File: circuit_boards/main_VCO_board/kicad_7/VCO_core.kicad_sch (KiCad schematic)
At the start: 46 parts, among them Q201 MMBT3904, SW2 SR1712F-0204, U1004 LM4040C-2.5, U6 SSI2130, U7 TL072

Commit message: Progress on circuit boards
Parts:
- R1001: value ? -> 1k
- R214: value ? -> 39k
- R215: value ? -> 47k
- R216, R217: value ? -> 2M2
- RV201: value ? -> 5k
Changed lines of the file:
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@@
   (title_block
     (title "MICRO-OX Main VCO board")
-    (date "2023-03-27")
+    (date "2023-04-12")
     (rev "0")
     (comment 2 "creativecommons.org/licenses/by/4.0")
@@
   )
   (text_box "Sync \"kick start\" circuit to ensure that the VCO starts up.\n\nSee Sound Semiconductor AB503 application brief."
-    (at 15.24 25.4 0) (size 29.21 21.59)
+    (at 15.24 25.4 0) (size 29.21 26.67)
     (stroke (width 0) (type default))
     (fill (type none))
@@
   (symbol (lib_id "Device:R") (at 86.36 173.99 270) (unit 1)
     (in_bom yes) (on_board yes) (dnp no) (fields_autoplaced)
-    (property "Reference" "R216" (at 86.36 167.64 90)
-      (effects (font (size 1.27 1.27)))
-    )
-    (property "Value" "?" (at 86.36 170.18 90)
+    (property "Reference" "R216" (at 86.36 168.91 90)
+      (effects (font (size 1.27 1.27)))
+    )
+    (property "Value" "2M2" (at 86.36 171.45 90)
       (effects (font (size 1.27 1.27)))
     )
@@
   (symbol (lib_id "Device:R_Potentiometer_Trim") (at 69.85 161.29 270) (unit 1)
     (in_bom yes) (on_board yes) (dnp no) (fields_autoplaced)
-    (property "Reference" "RV201" (at 69.85 154.94 90)
-      (effects (font (size 1.27 1.27)))
-    )
-    (property "Value" "?" (at 69.85 157.48 90)
+    (property "Reference" "RV201" (at 69.85 156.21 90)
+      (effects (font (size 1.27 1.27)))
+    )
+    (property "Value" "5k" (at 69.85 158.75 90)
       (effects (font (size 1.27 1.27)))
     )
@@
   (symbol (lib_id "Device:R") (at 86.36 147.32 270) (unit 1)
     (in_bom yes) (on_board yes) (dnp no) (fields_autoplaced)
-    (property "Reference" "R214" (at 86.36 140.97 90)
-      (effects (font (size 1.27 1.27)))
-    )
-    (property "Value" "?" (at 86.36 143.51 90)
+    (property "Reference" "R214" (at 86.36 142.24 90)
+      (effects (font (size 1.27 1.27)))
+    )
+    (property "Value" "39k" (at 86.36 144.78 90)
       (effects (font (size 1.27 1.27)))
     )
@@
   (symbol (lib_id "Device:R") (at 86.36 161.29 270) (unit 1)
     (in_bom yes) (on_board yes) (dnp no) (fields_autoplaced)
-    (property "Reference" "R215" (at 86.36 154.94 90)
-      (effects (font (size 1.27 1.27)))
-    )
-    (property "Value" "?" (at 86.36 157.48 90)
+    (property "Reference" "R215" (at 86.36 156.21 90)
+      (effects (font (size 1.27 1.27)))
+    )
+    (property "Value" "47k" (at 86.36 158.75 90)
       (effects (font (size 1.27 1.27)))
     )
@@
   (symbol (lib_id "Device:R") (at 86.36 185.42 270) (unit 1)
     (in_bom yes) (on_board yes) (dnp no) (fields_autoplaced)
-    (property "Reference" "R217" (at 86.36 179.07 90)
-      (effects (font (size 1.27 1.27)))
-    )
-    (property "Value" "?" (at 86.36 181.61 90)
+    (property "Reference" "R217" (at 86.36 180.34 90)
+      (effects (font (size 1.27 1.27)))
+    )
+    (property "Value" "2M2" (at 86.36 182.88 90)
       (effects (font (size 1.27 1.27)))
     )
@@
   (symbol (lib_id "Device:R") (at 128.27 163.83 0) (unit 1)
     (in_bom yes) (on_board yes) (dnp no) (fields_autoplaced)
-    (property "Reference" "R1001" (at 130.81 162.56 0)
-      (effects (font (size 1.27 1.27)) (justify left))
-    )
-    (property "Value" "?" (at 130.81 165.1 0)
-      (effects (font (size 1.27 1.27)) (justify left))
-    )
+    (property "Reference" "R1001" (at 130.81 163.195 0)
+      (effects (font (size 1.27 1.27)) (justify left))
+    )
+    (property "Value" "1k" (at 130.81 165.735 0)
+      (effects (font (size 1.27 1.27)) (justify left))
+    )

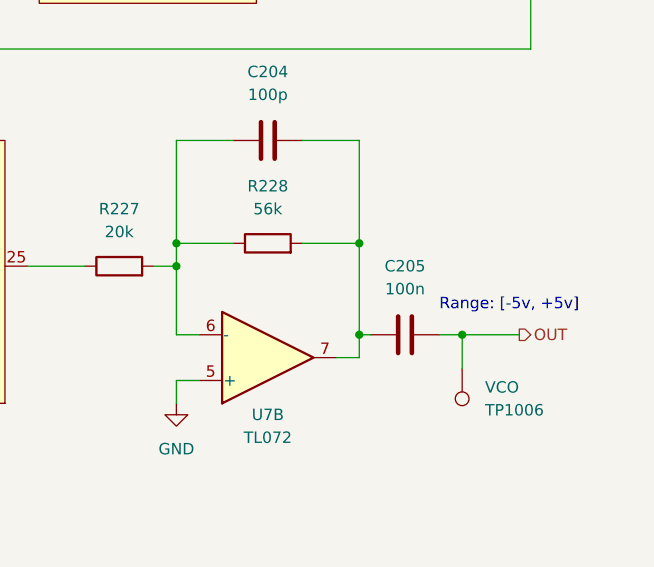
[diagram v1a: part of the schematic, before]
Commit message: Update PCBs, tweak vals, add VCF CV from DAC
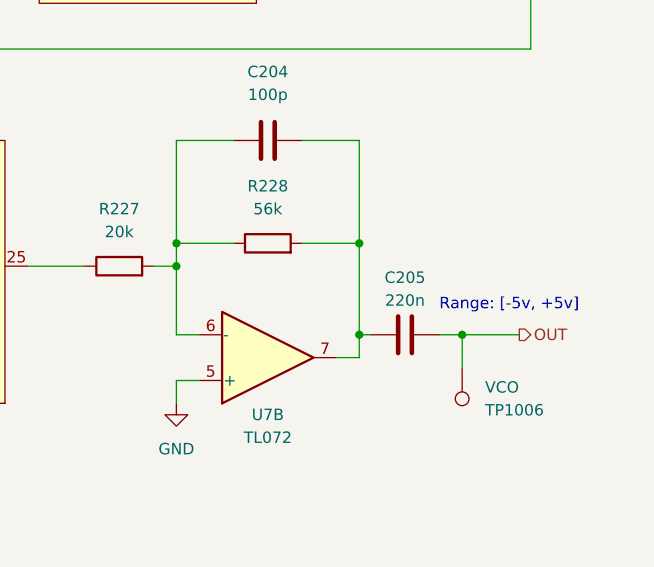
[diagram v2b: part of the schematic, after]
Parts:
- C205: value 100n -> 220n
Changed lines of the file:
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@@
   (symbol (lib_id "Device:C") (at 262.89 146.05 90) (unit 1)
     (in_bom yes) (on_board yes) (dnp no) (fields_autoplaced)
-    (property "Reference" "C205" (at 262.89 138.43 90)
+    (property "Reference" "C205" (at 262.89 139.7 90)
       (effects (font (size 1.27 1.27)))
     )
-    (property "Value" "100n" (at 262.89 140.97 90)
+    (property "Value" "220n" (at 262.89 142.24 90)
       (effects (font (size 1.27 1.27)))
     )

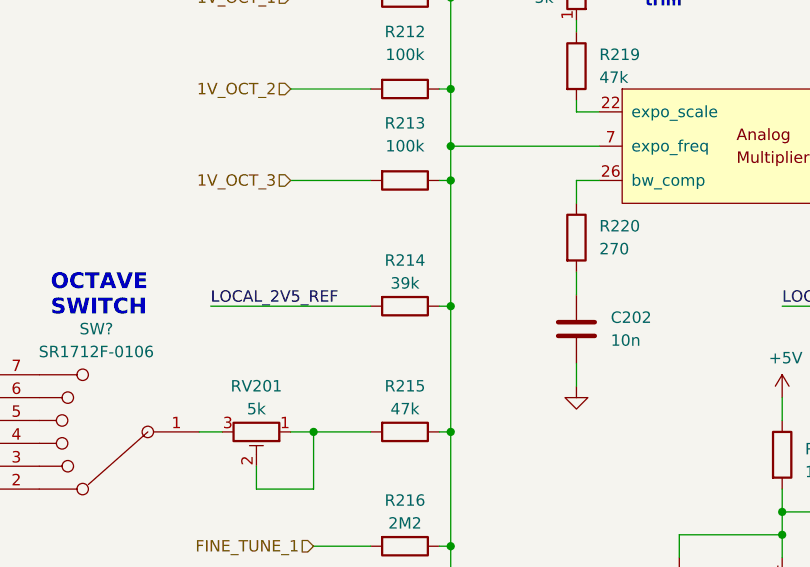
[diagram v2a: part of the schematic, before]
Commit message: Resistor tweaks while evaluating 1st build
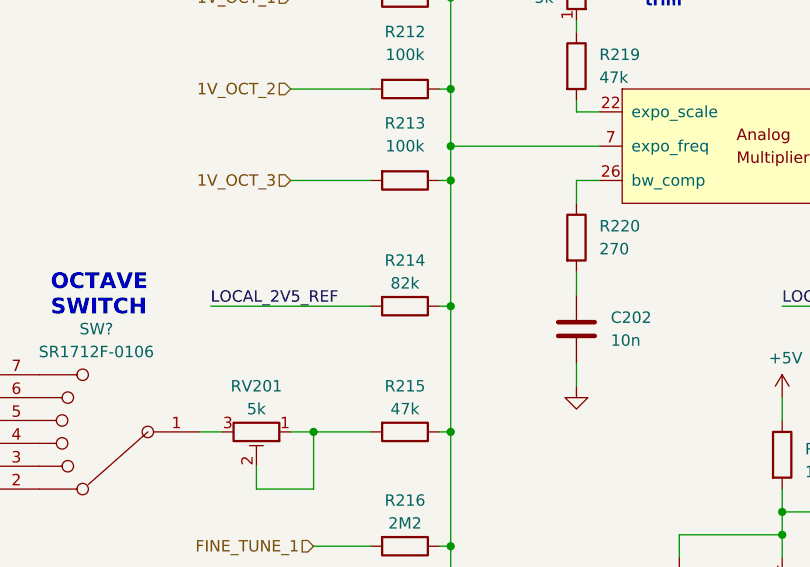
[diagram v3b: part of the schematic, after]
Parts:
- R214: value 39k -> 82k
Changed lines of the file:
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@@
       (effects (font (size 1.27 1.27)))
     )
-    (property "Value" "39k" (at 86.36 144.78 90)
+    (property "Value" "82k" (at 86.36 144.78 90)
       (effects (font (size 1.27 1.27)))
     )

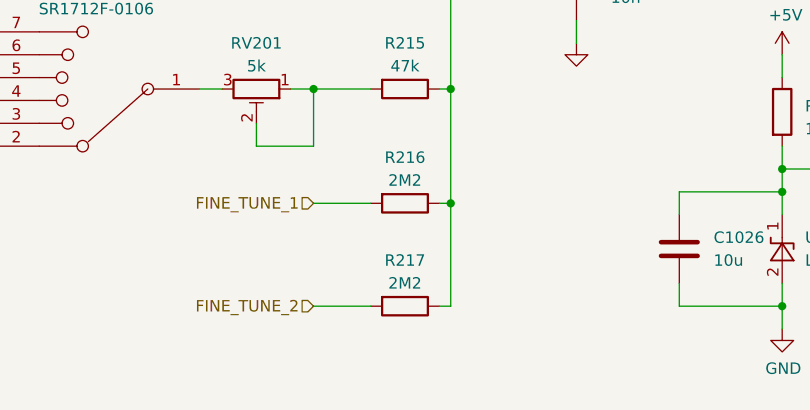
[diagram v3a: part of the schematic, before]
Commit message: Increase range of VCO B fine tune control
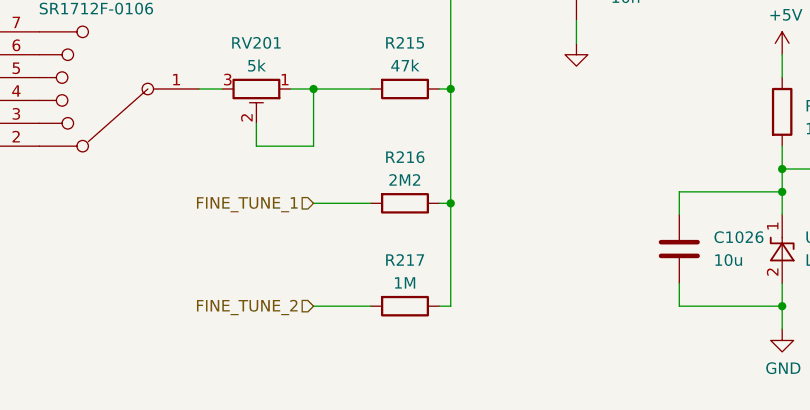
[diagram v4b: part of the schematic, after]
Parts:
- R217: value 2M2 -> 1M
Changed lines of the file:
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@@
       (effects (font (size 1.27 1.27)))
     )
-    (property "Value" "2M2" (at 86.36 182.88 90)
+    (property "Value" "1M" (at 86.36 182.88 90)
       (effects (font (size 1.27 1.27)))
     )
